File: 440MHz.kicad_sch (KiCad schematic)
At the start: 48 parts, among them J5 BWSMA-KWE-Z001, U10 74LVC1GU04DRL, U7 GRF5604, U9 SKYA21003

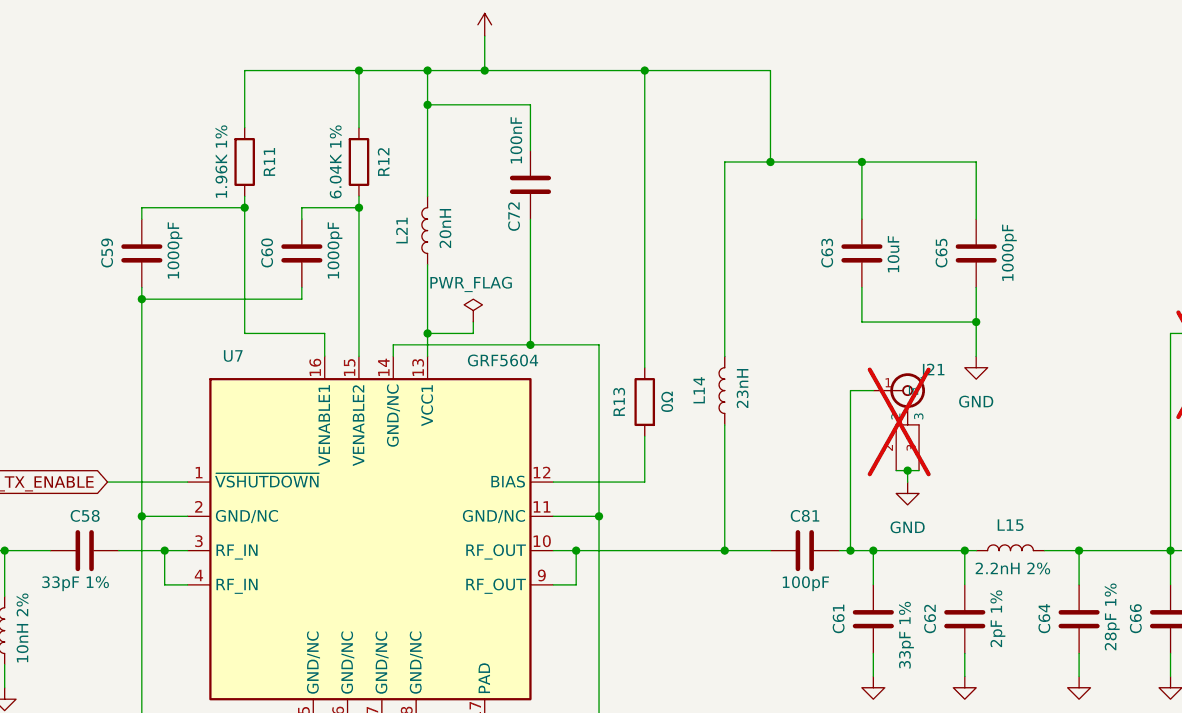
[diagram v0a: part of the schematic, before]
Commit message: Start working on BOM, fix supply indoctors
Signed-off-by: Corey Minyard <corey@minyard.net>
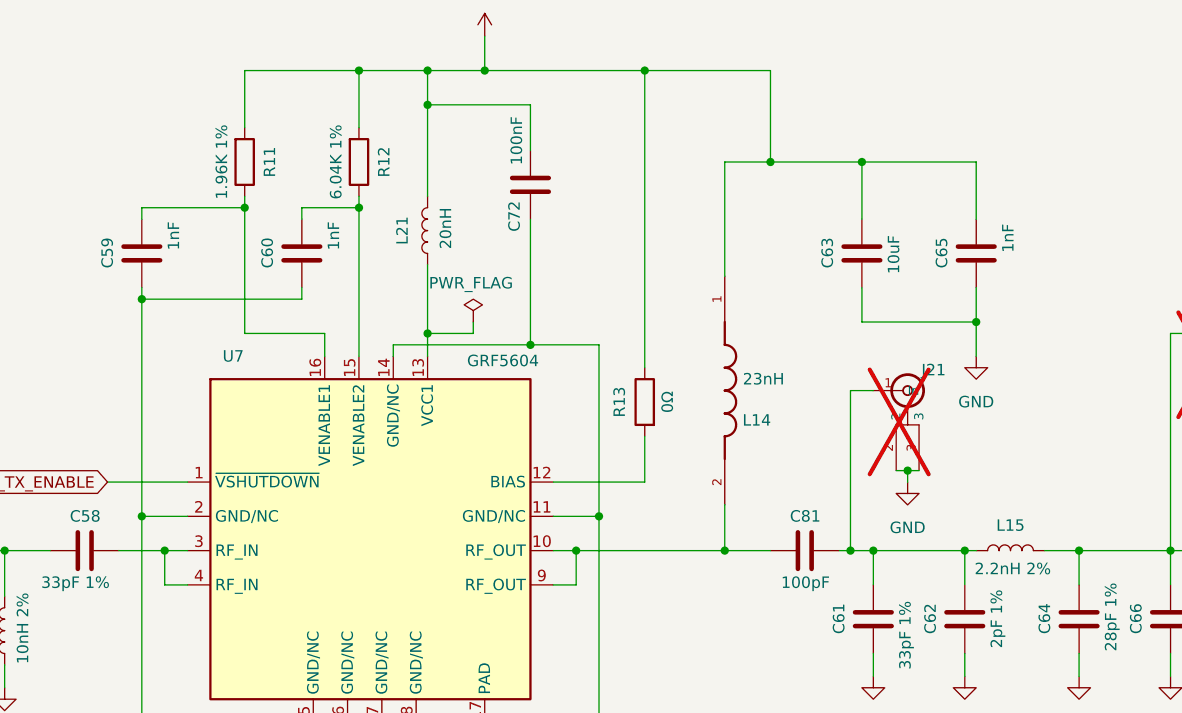
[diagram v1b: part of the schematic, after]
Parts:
- C59, C60, C65: value 1000pF -> 1nF
- C63: footprint Capacitor_SMD:C_0805_2012Metric_Pad1.18x1.45mm_HandSolder -> Capacitor_SMD:C_1206_3216Metric_Pad1.33x1.80mm_HandSolder
- L14: footprint Inductor_SMD:L_0603_1608Metric_Pad1.05x0.95mm_HandSolder -> footprints:IND_0908SQ-23NJLC; symbol Device:L -> Local Passives:0908SQ-23NJLC; Check_prices (none) -> https://www.snapeda.com/parts/0908SQ-23NJLC/Coilcraft/view-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; Description_1 (none) -> RF inductor, air core, 5% tol, SMT, RoHS; MANUFACTURER (none) -> Coilcraft; MAXIMUM_PACKAGE_HEIGHT (none) -> 2.032mm; MF (none) -> Coilcraft; MP (none) -> 0908SQ-23NJLC; PARTREV (none) -> 12/21/22; Package (none) -> None; Purchase-URL (none) -> https://www.snapeda.com/api/url_track_click_mouser/?unipart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; STANDARD (none) -> Manufacturer Recommendations; SnapEDA_Link (none) -> https://www.snapeda.com/parts/0908SQ-23NJLC/Coilcraft/view-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
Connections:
- net +5V: now also L14.1; no longer L14.2
- net at C81.1, U7.10 (RF_OUT), U7.9 (RF_OUT): now also L14.2; no longer L14.1
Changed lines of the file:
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@@
 	(wire
 		(pts
+			(xy 207.01 73.66) (xy 207.01 78.74)
+		)
+		(stroke
+			(width 0)
+			(type default)
+		)
+	)
+	(wire
+		(pts
 			(xy 170.18 55.88) (xy 185.42 55.88)
 		)
@@
 	(wire
 		(pts
+			(xy 207.01 48.26) (xy 207.01 35.56)
+		)
+		(stroke
+			(width 0)
+			(type default)
+		)
+	)
+	(wire
+		(pts
 			(xy 105.41 57.15) (xy 106.68 57.15)
 		)
@@
 	(wire
 		(pts
-			(xy 207.01 57.15) (xy 207.01 35.56)
-		)
-		(stroke
-			(width 0)
-			(type default)
-		)
-	)
-	(wire
-		(pts
 			(xy 220.98 60.96) (xy 223.52 60.96)
 		)
@@
 	(wire
 		(pts
-			(xy 207.01 64.77) (xy 207.01 78.74)
-		)
-		(stroke
-			(width 0)
-			(type default)
-		)
-	)
-	(wire
-		(pts
 			(xy 72.39 128.27) (xy 72.39 153.67)
 		)
@@
 	)
 	(symbol
-		(lib_id "Device:L")
-		(at 207.01 60.96 180)
+		(lib_id "Local Passives:0908SQ-23NJLC")
+		(at 207.01 60.96 270)
 		(unit 1)
 		(exclude_from_sim no)
@@
 		(dnp no)
 		(property "Reference" "L14"
-			(at 204.216 60.96 90)
+			(at 210.566 64.262 90)
 			(effects
 				(font
@@
 		)
 		(property "Value" "23nH"
-			(at 209.042 60.706 90)
+			(at 211.328 59.69 90)
 			(effects
 				(font
@@
 			)
 		)
-		(property "Footprint" "Inductor_SMD:L_0603_1608Metric_Pad1.05x0.95mm_HandSolder"
-			(at 207.01 60.96 0)
+		(property "Footprint" "footprints:IND_0908SQ-23NJLC"
+			(at 191.516 61.214 0)
 			(effects
 				(font
 					(size 1.27 1.27)
 				)
+				(justify bottom)
 				(hide yes)
 			)
@@
 			)
 		)
+		(property "DigiKey_Part_Number" ""
+			(at 207.01 60.96 0)
+			(effects
+				(font
+					(size 1.27 1.27)
+				)
+				(justify bottom)
+				(hide yes)
+			)
+		)
+		(property "MF" "Coilcraft"
+			(at 214.63 59.944 0)
+			(effects
+				(font
+					(size 1.27 1.27)
+				)
+				(justify bottom)
+				(hide yes)
+			)
+		)
+		(property "MAXIMUM_PACKAGE_HEIGHT" "2.032mm"
+			(at 211.836 60.96 0)
+			(effects
+				(font
+					(size 1.27 1.27)
+				)
+				(justify bottom)
+				(hide yes)
+			)
+		)
+		(property "Package" "None"
+			(at 216.662 69.342 0)
+			(effects
+				(font
+					(size 1.27 1.27)
+				)
+				(justify bottom)
+				(hide yes)
+			)
+		)
+		(property "Check_prices" "https://www.snapeda.com/parts/0908SQ-23NJLC/Coilcraft/view-part/?ref=eda"
+			(at 201.93 60.96 0)
+			(effects
+				(font
+					(size 1.27 1.27)
+				)
+				(justify bottom)
+				(hide yes)
+			)
+		)
+		(property "STANDARD" "Manufacturer Recommendations"
+			(at 188.214 61.722 0)
+			(effects
+				(font
+					(size 1.27 1.27)
+				)
+				(justify bottom)
+				(hide yes)
+			)
+		)
+		(property "PARTREV" "12/21/22"
+			(at 216.662 59.182 0)
+			(effects
+				(font
+					(size 1.27 1.27)
+				)
+				(justify bottom)
+				(hide yes)
+			)
+		)
+		(property "SnapEDA_Link" "https://www.snapeda.com/parts/0908SQ-23NJLC/Coilcraft/view-part/?ref=snap"
+			(at 199.136 60.706 0)
+			(effects
+				(font
+					(size 1.27 1.27)
+				)
+				(justify bottom)
+				(hide yes)
+			)
+		)
+		(property "MP" "0908SQ-23NJLC"
+			(at 185.674 61.214 0)
+			(effects
+				(font
+					(size 1.27 1.27)
+				)
+				(justify bottom)
+				(hide yes)
+			)
+		)
+		(property "Purchase-URL" "https://www.snapeda.com/api/url_track_click_mouser/?unipart_id=1604741&manufacturer=Coilcraft&part_name=0908SQ-23NJLC&search_term=0908sq-23njlc"
+			(at 196.85 60.96 0)
+			(effects
+				(font
+					(size 1.27 1.27)
+				)
+				(justify bottom)
+				(hide yes)
+			)
+		)
+		(property "Description_1" "RF inductor, air core, 5% tol, SMT, RoHS"
+			(at 194.31 60.706 0)
+			(effects
+				(font
+					(size 1.27 1.27)
+				)
+				(justify bottom)
+				(hide yes)
+			)
+		)
+		(property "MANUFACTURER" "Coilcraft"
+			(at 219.71 60.198 0)
+			(effects
+				(font
+					(size 1.27 1.27)
+				)
+				(justify bottom)
+				(hide yes)
+			)
+		)
 		(pin "1"
 		)
@@
 			)
 		)
-		(property "Value" "1000pF"
+		(property "Value" "1nF"
 			(at 238.506 42.418 90)
 			(effects
@@
 			)
 		)
-		(property "Value" "1000pF"
+		(property "Value" "1nF"
 			(at 163.576 42.164 90)
 			(effects
@@
 			)
 		)
-		(property "Value" "1000pF"
+		(property "Value" "1nF"
 			(at 145.796 42.164 90)
 			(effects
@@
 			)
 		)
-		(property "Footprint" "Capacitor_SMD:C_0805_2012Metric_Pad1.18x1.45mm_HandSolder"
+		(property "Footprint" "Capacitor_SMD:C_1206_3216Metric_Pad1.33x1.80mm_HandSolder"
 			(at 221.2848 41.91 0)
 			(effects

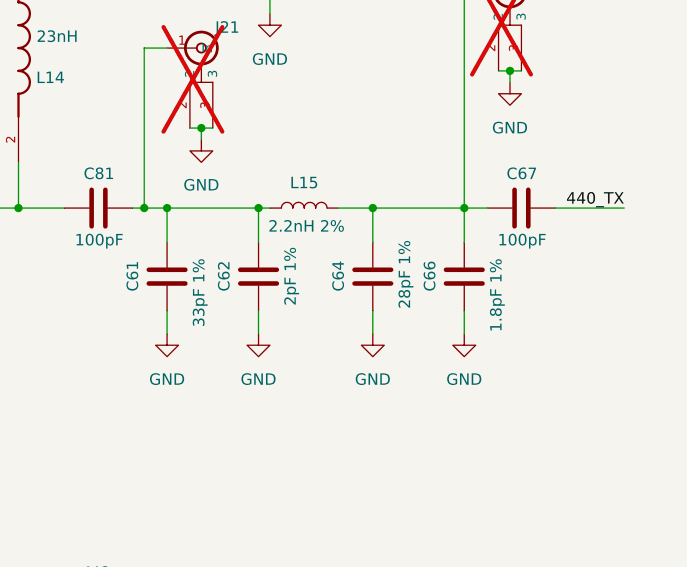
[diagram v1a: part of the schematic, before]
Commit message: Fix the value of a capacitor
It was 27pF, not 28pF.

Signed-off-by: Corey Minyard <corey@minyard.net>
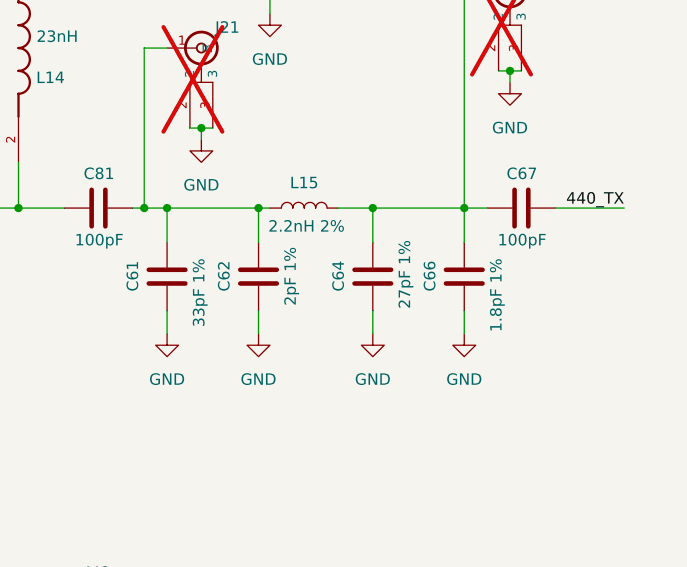
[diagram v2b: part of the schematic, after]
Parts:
- C64: value 28pF 1% -> 27pF 1%
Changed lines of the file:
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@@
 			)
 		)
-		(property "Value" "28pF 1%"
+		(property "Value" "27pF 1%"
 			(at 249.936 82.296 90)
 			(effects

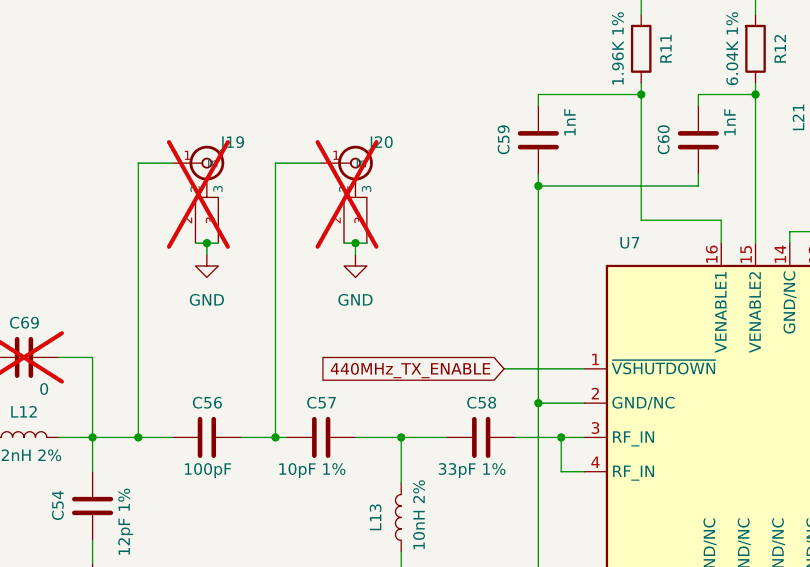
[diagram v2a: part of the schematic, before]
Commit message: Add pull up on the PA enables
So they are off by default.

Signed-off-by: Corey Minyard <corey@minyard.net>
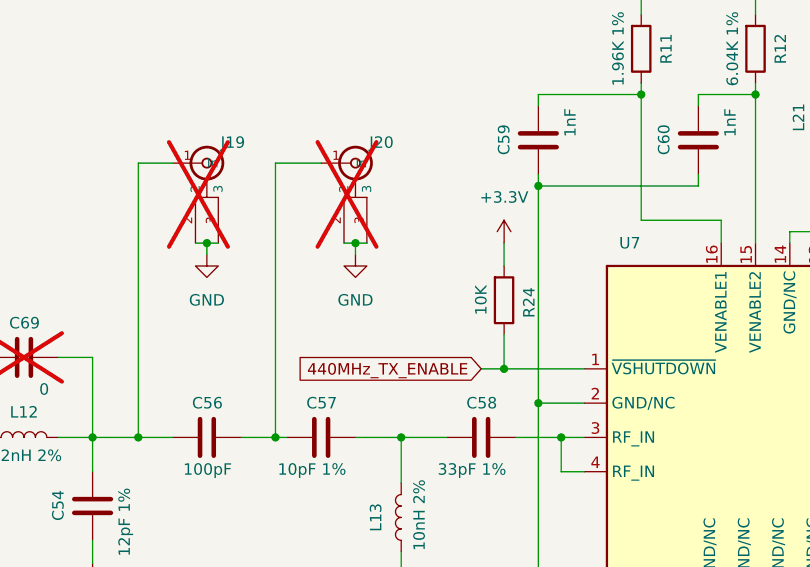
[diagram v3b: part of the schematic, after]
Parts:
- added R24: 10K, Resistor_SMD:R_0402_1005Metric, symbol Device:R
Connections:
- net +3.3V: now also R24.2
- net 440MHz_TX_ENABLE: now also R24.1
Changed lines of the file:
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@@
 	)
 	(junction
+		(at 138.43 71.12)
+		(diameter 0)
+		(color 0 0 0 0)
+	)
+	(junction
 		(at 180.34 25.4)
 		(diameter 0)
@@
 	(wire
 		(pts
+			(xy 138.43 57.15) (xy 138.43 59.69)
+		)
+		(stroke
+			(width 0)
+			(type default)
+		)
+	)
+	(wire
+		(pts
 			(xy 207.01 73.66) (xy 207.01 78.74)
 		)
@@
 	(wire
 		(pts
+			(xy 138.43 67.31) (xy 138.43 71.12)
+		)
+		(stroke
+			(width 0)
+			(type default)
+		)
+	)
+	(wire
+		(pts
 			(xy 223.52 90.17) (xy 223.52 92.71)
 		)
@@
 	(wire
 		(pts
+			(xy 138.43 71.12) (xy 147.32 71.12)
+		)
+		(stroke
+			(width 0)
+			(type default)
+		)
+	)
+	(wire
+		(pts
 			(xy 165.1 97.79) (xy 165.1 104.14)
 		)
@@
 	(wire
 		(pts
-			(xy 138.43 71.12) (xy 147.32 71.12)
+			(xy 135.89 71.12) (xy 138.43 71.12)
 		)
 		(stroke
@@
 	(global_label "440MHz_TX_ENABLE"
 		(shape input)
-		(at 138.43 71.12 180)
+		(at 135.89 71.12 180)
 		(fields_autoplaced yes)
 		(effects
@@
 		)
 		(property "Intersheetrefs" "${INTERSHEET_REFS}"
-			(at 116.8788 71.12 0)
+			(at 114.3388 71.12 0)
 			(effects
 				(font
@@
 	)
 	(symbol
+		(lib_id "Device:R")
+		(at 138.43 63.5 0)
+		(mirror x)
+		(unit 1)
+		(exclude_from_sim no)
+		(in_bom yes)
+		(on_board yes)
+		(dnp no)
+		(property "Reference" "R24"
+			(at 141.224 63.754 90)
+			(effects
+				(font
+					(size 1.27 1.27)
+				)
+			)
+		)
+		(property "Value" "10K"
+			(at 135.89 63.5 90)
+			(effects
+				(font
+					(size 1.27 1.27)
+				)
+			)
+		)
+		(property "Footprint" "Resistor_SMD:R_0402_1005Metric"
+			(at 136.652 63.5 90)
+			(effects
+				(font
+					(size 1.27 1.27)
+				)
+				(hide yes)
+			)
+		)
+		(property "Datasheet" "~"
+			(at 138.43 63.5 0)
+			(effects
+				(font
+					(size 1.27 1.27)
+				)
+				(hide yes)
+			)
+		)
+		(property "Description" "Resistor"
+			(at 138.43 63.5 0)
+			(effects
+				(font
+					(size 1.27 1.27)
+				)
+				(hide yes)
+			)
+		)
+		(pin "2"
+		)
+		(pin "1"
+		)
+		(instances
+			(project "FSKGroundStation"
+				(path "/23e49ab9-97e0-460a-806c-ff6f37958474/02f68d56-1c9b-4a2b-b713-a6f1b66ebbf1"
+					(reference "R24")
+					(unit 1)
+				)
+			)
+		)
+	)
+	(symbol
 		(lib_id "power:GND")
 		(at 276.86 151.13 0)
@@
 					(unit 1)
 				)
+			)
+		)
+	)
+	(symbol
+		(lib_id "power:+12V")
+		(at 138.43 57.15 0)
+		(unit 1)
+		(exclude_from_sim no)
+		(in_bom yes)
+		(on_board yes)
+		(dnp no)
+		(fields_autoplaced yes)
+		(property "Reference" "#PWR0106"
+			(at 138.43 60.96 0)
+			(effects
+				(font
+					(size 1.27 1.27)
+				)
+				(hide yes)
+			)
+		)
+		(property "Value" "+3.3V"
+			(at 138.43 52.07 0)
+			(effects
+				(font
+					(size 1.27 1.27)
+				)
+			)
+		)
+		(property "Footprint" ""
+			(at 138.43 57.15 0)
+			(effects
+				(font
+					(size 1.27 1.27)
+				)
+				(hide yes)
+			)
+		)
+		(property "Datasheet" ""
+			(at 138.43 57.15 0)
+			(effects
+				(font
+					(size 1.27 1.27)
+				)
+				(hide yes)
+			)
+		)
+		(property "Description" "Power symbol creates a global label with name \"+12V\""
+			(at 138.43 57.15 0)
+			(effects
+				(font
+					(size 1.27 1.27)
+				)
+				(hide yes)
+			)
+		)
+		(pin "1"
+		)
+		(instances
+			(project "FSKGroundStation"
+				(path "/23e49ab9-97e0-460a-806c-ff6f37958474/02f68d56-1c9b-4a2b-b713-a6f1b66ebbf1"
+					(reference "#PWR0106")
+					(unit 1)
+				)

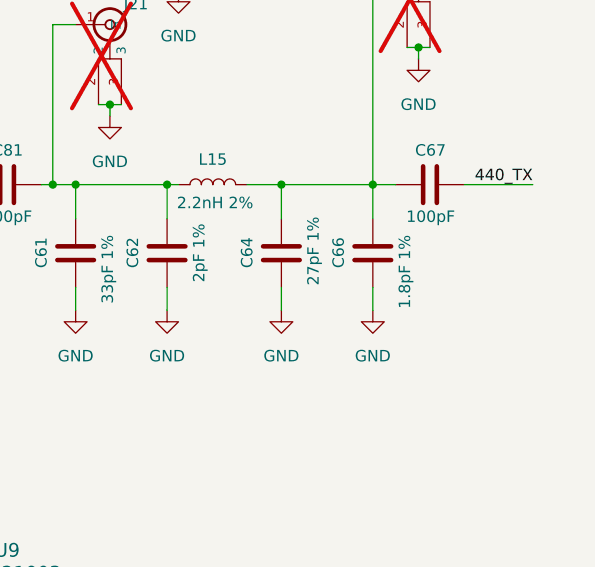
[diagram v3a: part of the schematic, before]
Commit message: Fix the 440 PA to work at 430-450
Signed-off-by: Corey Minyard <corey@minyard.net>
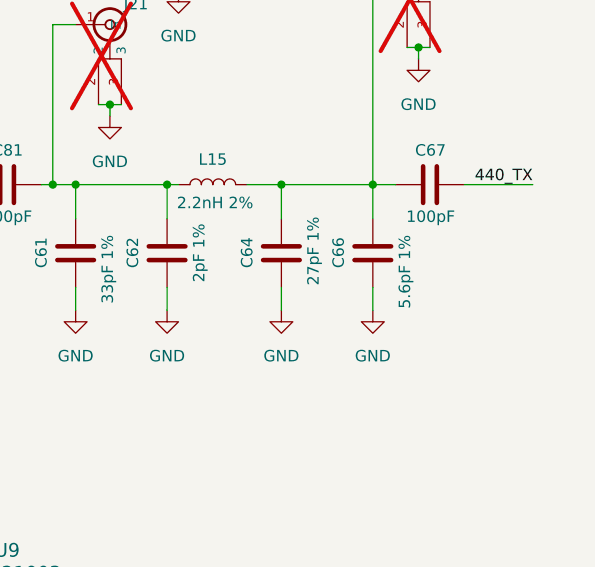
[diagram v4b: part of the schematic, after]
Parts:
- C66: value 1.8pF 1% -> 5.6pF 1%
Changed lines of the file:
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@@
 			)
 		)
-		(property "Value" "1.8pF 1%"
+		(property "Value" "5.6pF 1%"
 			(at 260.096 84.328 90)
 			(effects

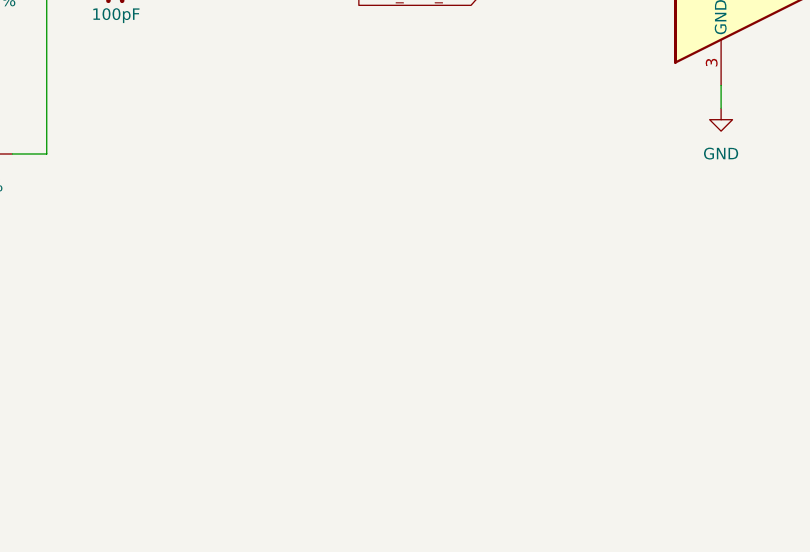
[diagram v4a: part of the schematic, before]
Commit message: Add thermsistors by the PAs
Signed-off-by: Corey Minyard <corey@minyard.net>
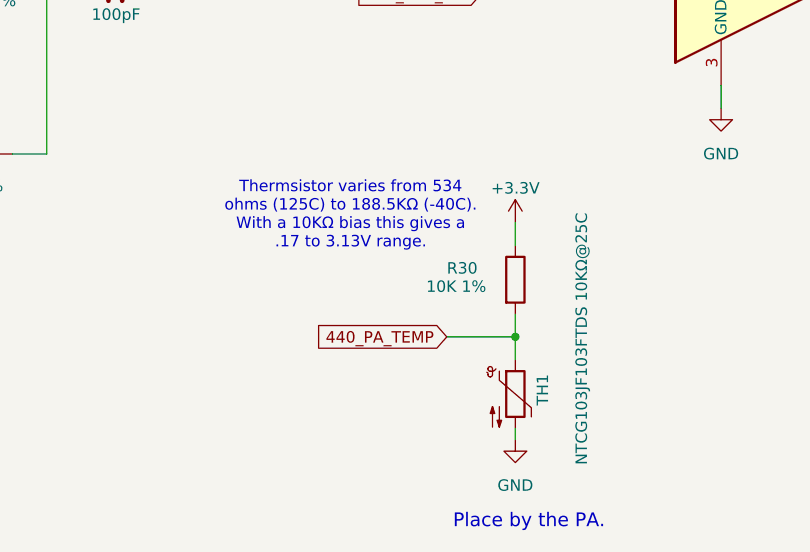
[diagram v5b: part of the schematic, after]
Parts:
- added R30: 10K 1%, Resistor_SMD:R_0402_1005Metric_Pad0.72x0.64mm_HandSolder, symbol Device:R
- added TH1: NTCG103JF103FTDS 10KΩ@25C, Resistor_SMD:R_0402_1005Metric, symbol Device:Thermistor_NTC
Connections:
- net +3.3V: now also R30.1
- net GND: now also TH1.2
- new net 440_PA_TEMP: R30.2, TH1.1
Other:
- note added: "Place by the PA."
- note added: "Thermsistor varies from 534 ohms (125C) to 188.5KΩ (-40C). With a 10KΩ bias this gives a .17 to 3.13V range."
